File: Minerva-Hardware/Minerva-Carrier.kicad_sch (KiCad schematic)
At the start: 14 parts, among them J11 USB_C_Receptacle_USB2.0, Q2 RQ6E080AJ, U1 BQ25798

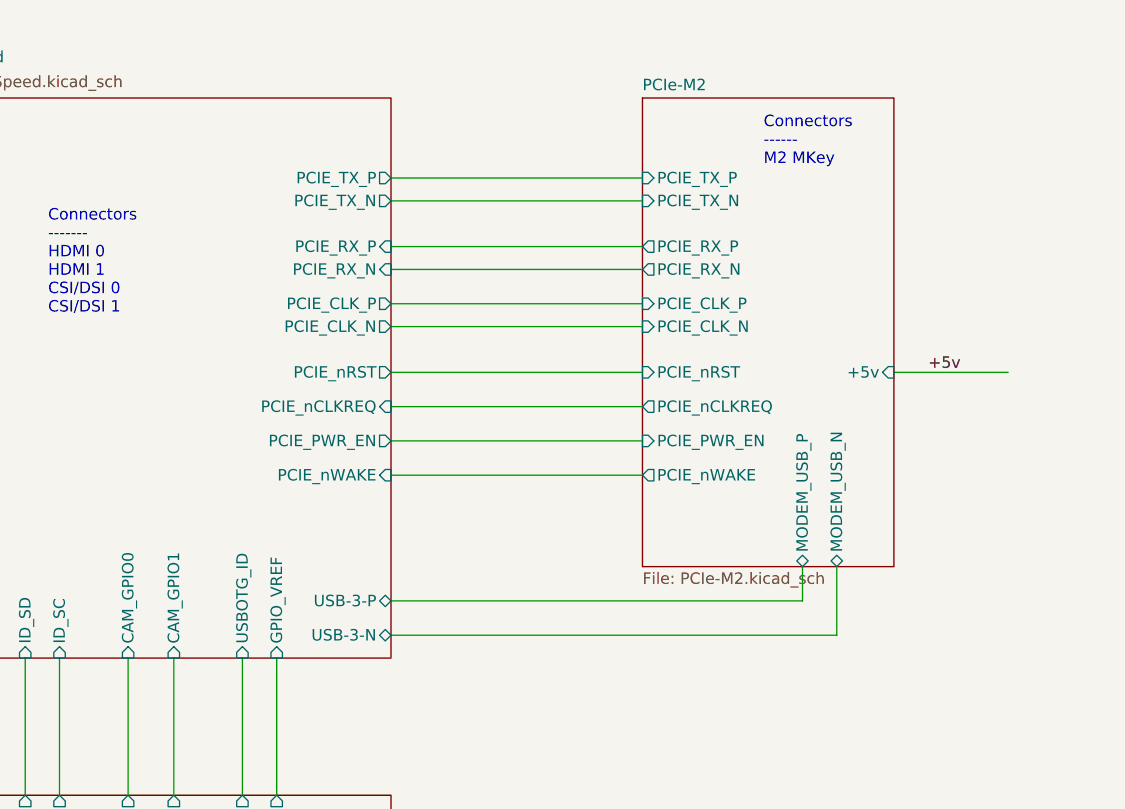
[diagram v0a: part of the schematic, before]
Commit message: Adding in the M.2 B WWAN
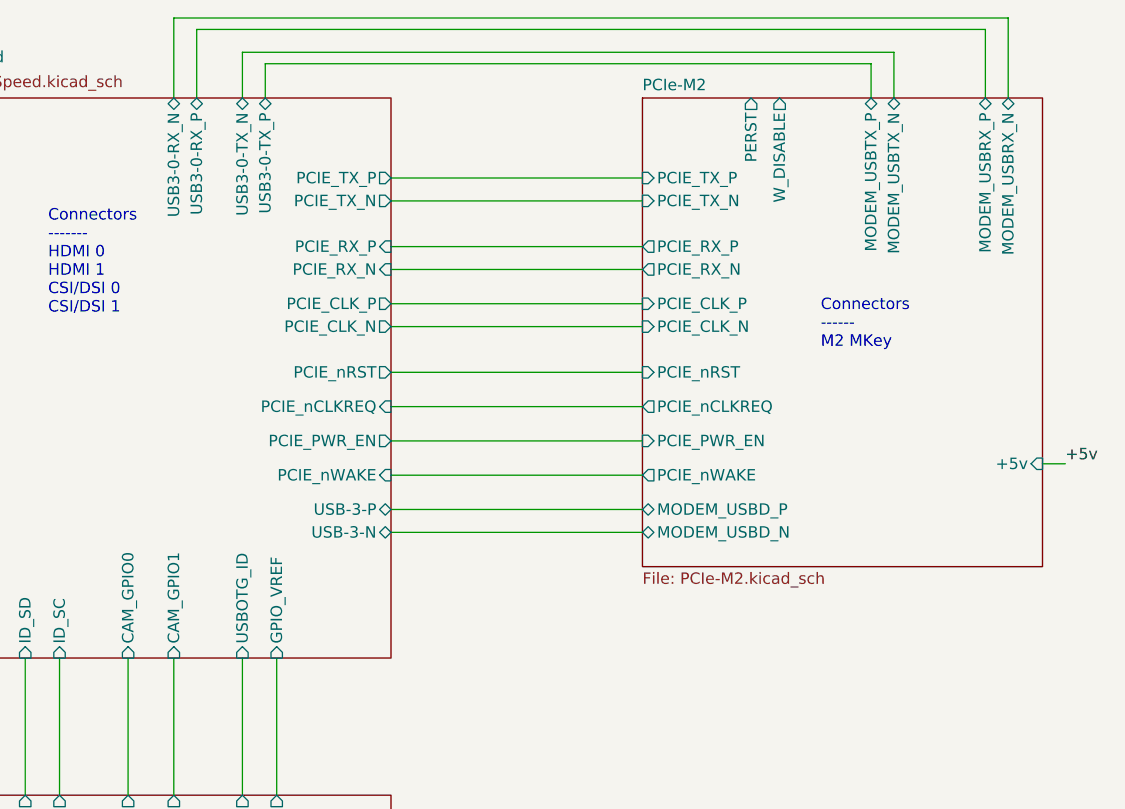
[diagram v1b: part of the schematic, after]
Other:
- sheet CM5_HighSpeed ports: added USB3-0-RX_N, USB3-0-RX_P, USB3-0-TX_N, USB3-0-TX_P; removed none
- sheet PCIe-M2 ports: added MODEM_USBD_N, MODEM_USBD_P, MODEM_USBRX_N, MODEM_USBRX_P, MODEM_USBTX_N, MODEM_USBTX_P, PERST, W_DISABLE; removed MODEM_USB_N, MODEM_USB_P
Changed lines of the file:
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@@
 	(text "Connectors\n------\nM2 MKey"
 		(exclude_from_sim no)
-		(at 228.092 41.91 0)
+		(at 234.442 62.23 0)
 		(effects
 			(font
@@
 	(wire
 		(pts
-			(xy 236.22 93.98) (xy 236.22 86.36)
+			(xy 186.69 130.81) (xy 195.58 130.81)
 		)
 		(stroke
@@
 	(wire
 		(pts
-			(xy 186.69 130.81) (xy 195.58 130.81)
+			(xy 173.99 96.52) (xy 173.99 111.76)
 		)
 		(stroke
 			(width 0)
-			(type default)
+			(type solid)
 		)
 	)
 	(wire
 		(pts
-			(xy 173.99 96.52) (xy 173.99 111.76)
+			(xy 113.03 48.26) (xy 129.54 48.26)
 		)
 		(stroke
@@
 	(wire
 		(pts
-			(xy 113.03 48.26) (xy 129.54 48.26)
+			(xy 162.56 168.91) (xy 162.56 170.18)
 		)
 		(stroke
 			(width 0)
-			(type solid)
+			(type default)
 		)
 	)
 	(wire
 		(pts
-			(xy 162.56 168.91) (xy 162.56 170.18)
+			(xy 242.57 29.21) (xy 170.18 29.21)
 		)
 		(stroke
@@
 	(wire
 		(pts
+			(xy 186.69 80.01) (xy 214.63 80.01)
+		)
+		(stroke
+			(width 0)
+			(type default)
+		)
+	)
+	(wire
+		(pts
 			(xy 107.95 147.32) (xy 95.25 147.32)
 		)
@@
 	(wire
 		(pts
+			(xy 172.72 34.29) (xy 172.72 30.48)
+		)
+		(stroke
+			(width 0)
+			(type default)
+		)
+	)
+	(wire
+		(pts
 			(xy 125.73 130.81) (xy 129.54 130.81)
 		)
@@
 	(wire
 		(pts
-			(xy 232.41 90.17) (xy 232.41 86.36)
+			(xy 80.01 162.56) (xy 80.01 167.64)
 		)
 		(stroke
@@
 	(wire
 		(pts
-			(xy 80.01 162.56) (xy 80.01 167.64)
+			(xy 162.56 96.52) (xy 162.56 111.76)
 		)
 		(stroke
@@
 	(wire
 		(pts
-			(xy 162.56 96.52) (xy 162.56 111.76)
+			(xy 91.44 142.24) (xy 90.17 142.24)
 		)
 		(stroke
@@
 	(wire
 		(pts
-			(xy 91.44 142.24) (xy 90.17 142.24)
+			(xy 186.69 50.8) (xy 214.63 50.8)
 		)
 		(stroke
 			(width 0)
-			(type default)
+			(type solid)
 		)
 	)
 	(wire
 		(pts
-			(xy 186.69 50.8) (xy 214.63 50.8)
+			(xy 165.1 26.67) (xy 252.73 26.67)
 		)
 		(stroke
 			(width 0)
-			(type solid)
+			(type default)
 		)
 	)
@@
 	(wire
 		(pts
-			(xy 242.57 64.77) (xy 255.27 64.77)
+			(xy 261.62 74.93) (xy 259.08 74.93)
 		)
 		(stroke
@@
 	(wire
 		(pts
+			(xy 170.18 29.21) (xy 170.18 34.29)
+		)
+		(stroke
+			(width 0)
+			(type default)
+		)
+	)
+	(wire
+		(pts
+			(xy 240.03 30.48) (xy 240.03 34.29)
+		)
+		(stroke
+			(width 0)
+			(type default)
+		)
+	)
+	(wire
+		(pts
 			(xy 46.99 92.71) (xy 69.85 92.71)
 		)
@@
 	(wire
 		(pts
+			(xy 162.56 25.4) (xy 162.56 34.29)
+		)
+		(stroke
+			(width 0)
+			(type default)
+		)
+	)
+	(wire
+		(pts
 			(xy 43.18 82.55) (xy 46.99 82.55)
 		)
@@
 	(wire
 		(pts
+			(xy 172.72 30.48) (xy 240.03 30.48)
+		)
+		(stroke
+			(width 0)
+			(type default)
+		)
+	)
+	(wire
+		(pts
+			(xy 252.73 26.67) (xy 252.73 34.29)
+		)
+		(stroke
+			(width 0)
+			(type default)
+		)
+	)
+	(wire
+		(pts
+			(xy 186.69 82.55) (xy 214.63 82.55)
+		)
+		(stroke
+			(width 0)
+			(type default)
+		)
+	)
+	(wire
+		(pts
 			(xy 62.23 57.15) (xy 62.23 59.69)
 		)
@@
 	(wire
 		(pts
-			(xy 186.69 90.17) (xy 232.41 90.17)
+			(xy 165.1 34.29) (xy 165.1 26.67)
 		)
 		(stroke
@@
 	(wire
 		(pts
-			(xy 186.69 93.98) (xy 236.22 93.98)
+			(xy 255.27 25.4) (xy 162.56 25.4)
+		)
+		(stroke
+			(width 0)
+			(type default)
+		)
+	)
+	(wire
+		(pts
+			(xy 242.57 34.29) (xy 242.57 29.21)
 		)
 		(stroke
@@
 		)
 	)
+	(wire
+		(pts
+			(xy 255.27 34.29) (xy 255.27 25.4)
+		)
+		(stroke
+			(width 0)
+			(type default)
+		)
+	)
 	(label "+5v"
 		(at 72.39 72.39 0)
@@
 	)
 	(label "+5v"
-		(at 246.38 64.77 0)
+		(at 261.62 74.93 0)
 		(effects
 			(font
@@
 		)
 		(pin "USB-3-P" bidirectional
-			(at 186.69 90.17 0)
+			(at 186.69 80.01 0)
 			(effects
 				(font
@@
 		)
 		(pin "USB-3-N" bidirectional
-			(at 186.69 93.98 0)
+			(at 186.69 82.55 0)
+			(effects
+				(font
+					(size 1.27 1.27)
+				)
+				(justify right)
+			)
+		)
+		(pin "USB3-0-RX_N" bidirectional
+			(at 162.56 34.29 90)
+			(effects
+				(font
+					(size 1.27 1.27)
+				)
+				(justify right)
+			)
+		)
+		(pin "USB3-0-RX_P" bidirectional
+			(at 165.1 34.29 90)
+			(effects
+				(font
+					(size 1.27 1.27)
+				)
+				(justify right)
+			)
+		)
+		(pin "USB3-0-TX_N" bidirectional
+			(at 170.18 34.29 90)
+			(effects
+				(font
+					(size 1.27 1.27)
+				)
+				(justify right)
+			)
+		)
+		(pin "USB3-0-TX_P" bidirectional
+			(at 172.72 34.29 90)
 			(effects
 				(font
@@
 	(sheet
 		(at 214.63 34.29)
-		(size 27.94 52.07)
+		(size 44.45 52.07)
 		(exclude_from_sim no)
 		(in_bom yes)
@@
 		)
 		(pin "+5v" input
-			(at 242.57 64.77 0)
+			(at 259.08 74.93 0)
 			(effects
 				(font
@@
 			)
 		)
-		(pin "MODEM_USB_N" bidirectional
-			(at 236.22 86.36 270)
+		(pin "W_DISABLE" output
+			(at 229.87 34.29 90)
+			(effects
+				(font
+					(size 1.27 1.27)
+				)
+				(justify right)
+			)
+		)
+		(pin "PERST" output
+			(at 226.7012 34.29 90)
+			(effects
+				(font
+					(size 1.27 1.27)
+				)
+				(justify right)
+			)
+		)
+		(pin "MODEM_USBD_N" bidirectional
+			(at 214.63 82.55 180)
 			(effects
 				(font
@@
 			)
 		)
-		(pin "MODEM_USB_P" bidirectional
-			(at 232.41 86.36 270)
+		(pin "MODEM_USBD_P" bidirectional
+			(at 214.63 80.01 180)
 			(effects
 				(font
@@
 			)
 		)
+		(pin "MODEM_USBRX_N" bidirectional
+			(at 255.27 34.29 90)
+			(effects
+				(font
+					(size 1.27 1.27)
+				)
+				(justify right)
+			)
+		)
+		(pin "MODEM_USBRX_P" bidirectional
+			(at 252.73 34.29 90)
+			(effects
+				(font
+					(size 1.27 1.27)
+				)
+				(justify right)
+			)
+		)
+		(pin "MODEM_USBTX_N" bidirectional
+			(at 242.57 34.29 90)
+			(effects
+				(font
+					(size 1.27 1.27)
+				)
+				(justify right)
+			)
+		)
+		(pin "MODEM_USBTX_P" bidirectional
+			(at 240.03 34.29 90)
+			(effects
+				(font
+					(size 1.27 1.27)
+				)
+				(justify right)
+			)
+		)

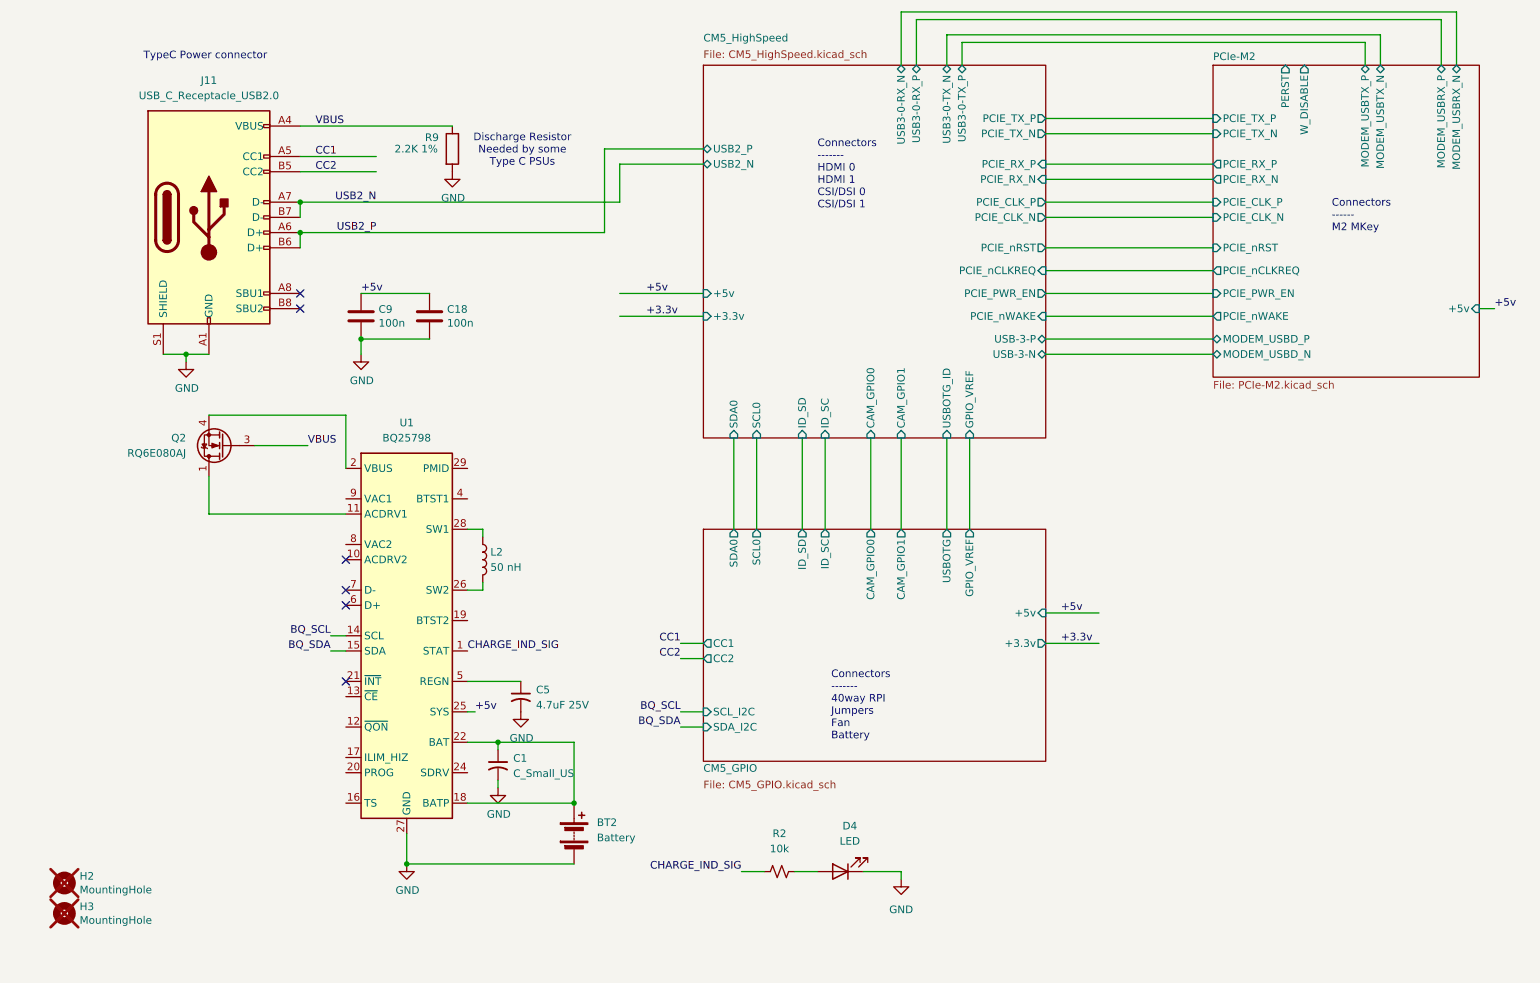
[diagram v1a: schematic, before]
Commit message: Redid the BQ powerpath unit
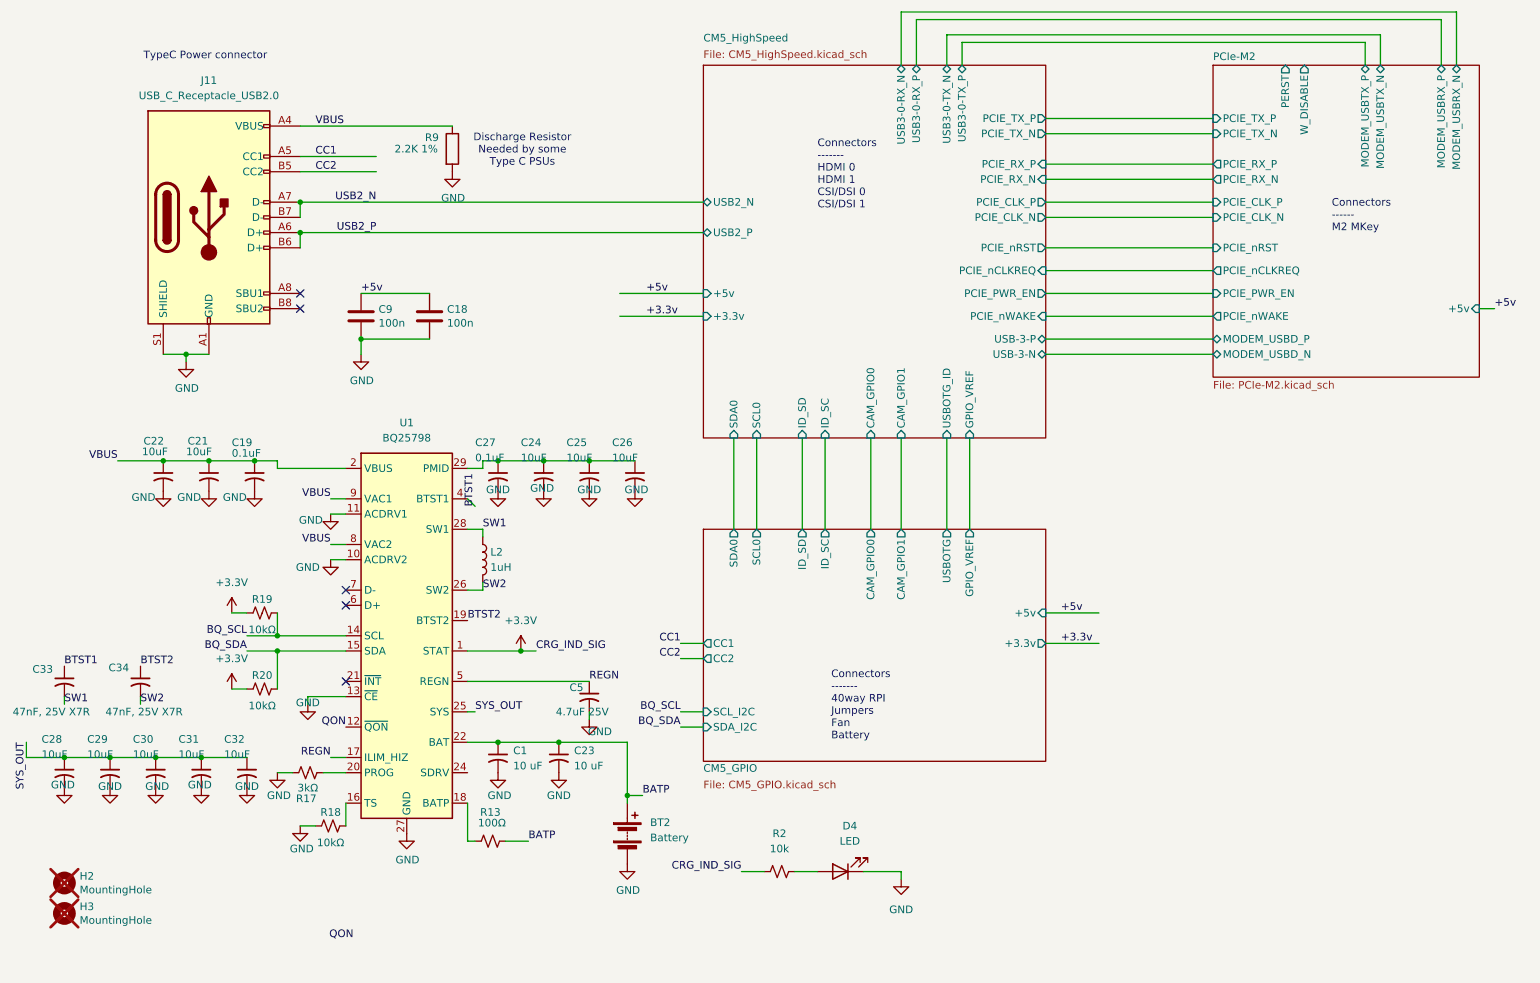
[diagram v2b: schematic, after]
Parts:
- removed Q2: RQ6E080AJ, Package_TO_SOT_SMD:TSOT-23-6, symbol Transistor_FET:RQ6E080AJ
- added C19, C27: 0.1uF, Capacitor_SMD:C_01005_0402Metric, symbol Device:C_Small_US
- added C21, C22, C24, C25, C26, C28, C29, C30, C31, C32: 10uF, Capacitor_SMD:C_01005_0402Metric, symbol Device:C_Small_US
- added C23: 10 uF, Capacitor_SMD:C_0201_0603Metric, symbol Device:C_Small_US
- added C33, C34: 47nF, 25V X7R, Capacitor_SMD:C_01005_0402Metric, symbol Device:C_Small_US
- added R13: 100Ω, symbol Device:R_Small_US
- added R17: 3kΩ, symbol Device:R_Small_US
- added R18, R19, R20: 10kΩ, symbol Device:R_Small_US
- C1: value C_Small_US -> 10 uF
- L2: value 50 nH -> 1uH
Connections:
- net +5v: no longer U1.25 (SYS)
- net BQ_SCL: now also R19.2
- net BQ_SDA: now also R20.2
- net GND: now also U1.10 (ACDRV2), U1.11 (ACDRV1), U1.13 (~{CE}), C19.2, C21.2, C22.2, C23.2, C24.2, C25.2, C26.2, C27.2, C28.2, C29.2, C30.2, C31.2, C32.2, R17.2, R18.1
- net VBUS: now also U1.2 (VBUS), U1.3 (VBUS), U1.8 (VAC2), U1.9 (VAC1), C19.1, C21.1, C22.1
- net BATP: now reaches BT2.1 (+), C1.1, U1.22 (BAT), U1.23 (BAT)
- net BATP: now also C23.1, R13.2; no longer U1.18 (BATP)
- net SW1: now reaches L2.1, U1.28 (SW1)
- net SW1: now also C33.2
- net SW2: now reaches L2.2, U1.26 (SW2)
- net SW2: now also C34.2
- net REGN: now reaches C5.1, U1.5 (REGN)
- net REGN: now also U1.17 (ILIM_HIZ)
- net QON: now reaches U1.12 (~{QON})
- net at U1.16 (TS): now also R18.2
- net BTST2: now reaches U1.19 (BTST2)
- net BTST2: now also C34.1
- net at U1.20 (PROG): now also R17.1
- net at U1.29 (PMID): now also C24.1, C25.1, C26.1, C27.1
- net BTST1: now reaches U1.4 (BTST1)
- net BTST1: now also C33.1
- net CHARGE_IND_SIG renamed +3.3V
- net +3.3V: now also R19.1, R20.1
- new net: R13.1, U1.18 (BATP)
- new net SYS_OUT: C28.1, C29.1, C30.1, C31.1, C32.1, U1.25 (SYS)
- no-connect marks 6 -> 5
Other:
- moved on the sheet: BT2, C1, C5

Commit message: working on pcb more
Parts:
- L2: footprint Inductor_THT:L_Axial_L5.3mm_D2.2mm_P7.62mm_Horizontal_Vishay_IM-1 -> CM5 IO Board-rev2:L_Bourns_SRP5030CC
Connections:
- no-connect marks 5 -> 6
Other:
- sheet CM5_GPIO ports: added none; removed USBOTG
- sheet CM5_HighSpeed ports: added USB-3_N, USB-3_P; removed USB-3-N, USB-3-P, USBOTG_ID
- moved on the sheet: R2, R9
